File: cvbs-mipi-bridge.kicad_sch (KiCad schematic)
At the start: 114 parts, among them IC1 ADV7282-M, IC2 TLV70018, IC4 SN74AUP1G17DCKR, IC5 SN74AUP1G17DCKR, J1 WE_68715014522, J2 1053131102, J3 KLPX-0848A-2-Y, J4 KLPX-0848A-2-Y, J5 KLPX-0848A-2-Y, J6 KLPX-0848A-2-Y, J7 61300211121, Q1 BSS138PW, Q2 BSS138PW, Q3 BSS138PW, Q4 BSS138PW, Y1 ABM8G-28.63636MHZ-18-D2Y-T

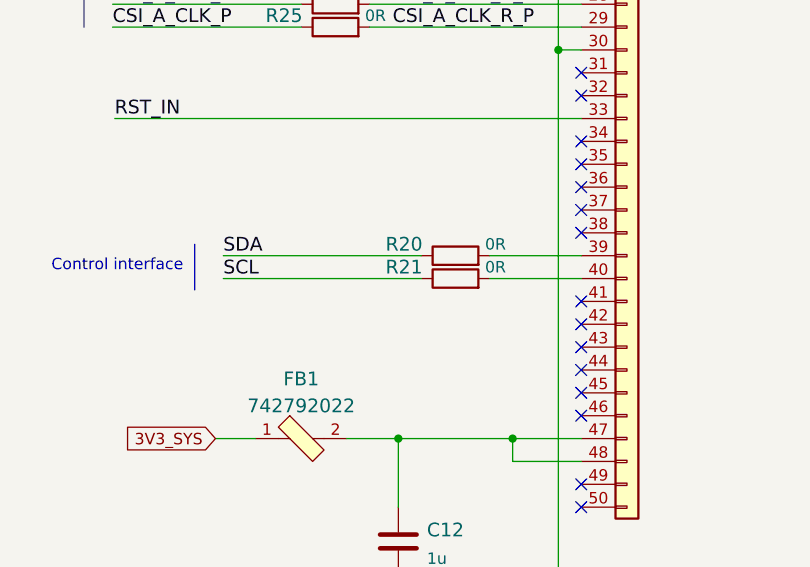
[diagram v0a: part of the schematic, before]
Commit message: Add second pair of resistors for re-connecting I2C.
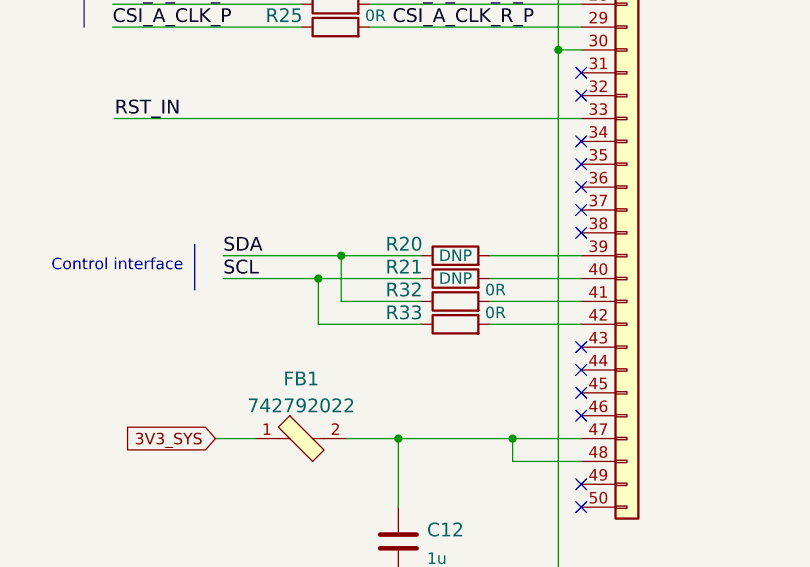
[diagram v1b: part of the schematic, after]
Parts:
- added R32, R33: R_0R_0402, cvbs-mipi-bridge-footprints:0402-res, symbol cvbs-mipi-bridge:R_0R_0402
- R20, R21: DNP (none) -> DNP
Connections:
- net SCL: now also R33.1
- net SDA: now also R32.1
- net at J1.41 (Pin_41): now also R32.2
- net at J1.42 (Pin_42): now also R33.2
- no-connect marks 35 -> 33
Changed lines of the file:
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@@
   (junction (at 363.855 155.575) (diameter 0) (color 0 0 0 0)
   )
+  (junction (at 357.505 135.255) (diameter 0) (color 0 0 0 0)
+  )
   (junction (at 193.04 50.8) (diameter 0) (color 0 0 0 0)
   )
@@
   (junction (at 381.635 74.295) (diameter 0) (color 0 0 0 0)
   )
+  (junction (at 354.965 137.795) (diameter 0) (color 0 0 0 0)
+  )
   (junction (at 113.03 36.83) (diameter 0) (color 0 0 0 0)
   )
@@
   (no_connect (at 384.175 51.435))
   (no_connect (at 384.175 56.515))
-  (no_connect (at 384.175 140.335))
-  (no_connect (at 384.175 142.875))
   (no_connect (at 384.175 86.995))
   (no_connect (at 384.175 92.075))
@@
     (stroke (width 0) (type default) (color 0 0 0 0))
   )
+  (wire (pts (xy 357.505 140.335) (xy 357.505 135.255))
+    (stroke (width 0) (type default) (color 0 0 0 0))
+  )
   (wire (pts (xy 114.935 97.79) (xy 136.525 97.79))
     (stroke (width 0) (type default) (color 0 0 0 0))
@@
     (stroke (width 0) (type default) (color 0 0 0 0))
   )
+  (wire (pts (xy 366.395 142.875) (xy 354.965 142.875))
+    (stroke (width 0) (type default) (color 0 0 0 0))
+  )
   (wire (pts (xy 275.59 86.995) (xy 276.86 86.995))
     (stroke (width 0) (type default) (color 0 0 0 0))
@@
     (stroke (width 0) (type default) (color 0 0 0 0))
   )
+  (wire (pts (xy 374.015 142.875) (xy 384.175 142.875))
+    (stroke (width 0) (type default) (color 0 0 0 0))
+  )
   (wire (pts (xy 122.555 113.03) (xy 104.775 113.03))
     (stroke (width 0) (type default) (color 0 0 0 0))
@@
     (stroke (width 0) (type default) (color 0 0 0 0))
   )
+  (wire (pts (xy 374.015 140.335) (xy 384.175 140.335))
+    (stroke (width 0) (type default) (color 0 0 0 0))
+  )
   (wire (pts (xy 200.279 140.97) (xy 200.279 146.05))
     (stroke (width 0) (type default) (color 0 0 0 0))
@@
     (stroke (width 0) (type default) (color 0 0 0 0))
   )
-  (wire (pts (xy 344.4047 135.255) (xy 366.395 135.255))
+  (wire (pts (xy 344.4047 135.255) (xy 357.505 135.255))
     (stroke (width 0) (type default) (color 0 0 0 0))
   )
@@
     (stroke (width 0) (type default) (color 0 0 0 0))
   )
+  (wire (pts (xy 354.965 137.795) (xy 366.395 137.795))
+    (stroke (width 0) (type default) (color 0 0 0 0))
+  )
   (wire (pts (xy 288.29 168.275) (xy 288.29 170.815))
     (stroke (width 0) (type default) (color 0 0 0 0))
@@
     (stroke (width 0) (type default) (color 0 0 0 0))
   )
+  (wire (pts (xy 354.965 142.875) (xy 354.965 137.795))
+    (stroke (width 0) (type default) (color 0 0 0 0))
+  )
   (wire (pts (xy 384.175 74.295) (xy 381.635 74.295))
     (stroke (width 0) (type default) (color 0 0 0 0))
@@
     (stroke (width 0) (type default) (color 0 0 0 0))
   )
+  (wire (pts (xy 357.505 135.255) (xy 366.395 135.255))
+    (stroke (width 0) (type default) (color 0 0 0 0))
+  )
   (wire (pts (xy 133.985 92.71) (xy 136.525 92.71))
     (stroke (width 0) (type default) (color 0 0 0 0))
@@
     (stroke (width 0) (type default) (color 0 0 0 0))
   )
-  (wire (pts (xy 344.4047 137.795) (xy 366.395 137.795))
+  (wire (pts (xy 344.4047 137.795) (xy 354.965 137.795))
     (stroke (width 0) (type default) (color 0 0 0 0))
   )
@@
     (stroke (width 0) (type default) (color 0 0 0 0))
   )
+  (wire (pts (xy 366.395 140.335) (xy 357.505 140.335))
+    (stroke (width 0) (type default) (color 0 0 0 0))
+  )
   (wire (pts (xy 138.43 224.155) (xy 167.64 224.155))
     (stroke (width 0) (type default) (color 0 0 0 0))
@@
       (effects (font (size 1.524 1.524)) (justify left) hide)
     )
-    (property "Val" "0R" (id 6) (at 374.65 133.985 0))
+    (property "Val" "0R" (id 6) (at 374.65 133.985 0)
+      (effects (font (size 1.27 1.27)) hide)
+    )
+    (property "DNP" "DNP" (id 7) (at 370.205 135.255 0))
     (pin "1")
     (pin "2")
@@
     (pin "1")
   )
+  (symbol (lib_id "cvbs-mipi-bridge:R_0R_0402") (at 370.205 140.335 0) (unit 1)
+    (in_bom yes) (on_board yes)
+    (property "Reference" "R32" (id 0) (at 364.49 139.065 0)
+      (effects (font (size 1.524 1.524)))
+    )
+    (property "Value" "R_0R_0402" (id 1) (at 370.205 144.145 0)
+      (effects (font (size 1.524 1.524)) hide)
+    )
+    (property "Footprint" "cvbs-mipi-bridge-footprints:0402-res" (id 2) (at 375.285 135.255 0)
+      (effects (font (size 1.524 1.524)) (justify left) hide)
+    )
+    (property "Datasheet" "" (id 3) (at 370.205 140.335 0)
+      (effects (font (size 1.27 1.27)) hide)
+    )
+    (property "Manufacturer" "PANASONIC" (id 4) (at 375.285 130.175 0)
+      (effects (font (size 1.524 1.524)) (justify left) hide)
+    )
+    (property "MPN" "ERJ2GE0R00X" (id 5) (at 375.285 132.715 0)
+      (effects (font (size 1.524 1.524)) (justify left) hide)
+    )
+    (property "Val" "0R" (id 6) (at 374.65 139.065 0))
+    (pin "1")
+    (pin "2")
+  )
   (symbol (lib_id "cvbs-mipi-bridge:GND") (at 288.29 153.67 0) (unit 1)
     (in_bom yes) (on_board yes) (fields_autoplaced)
@@
     (pin "M")
   )
+  (symbol (lib_id "cvbs-mipi-bridge:R_0R_0402") (at 370.205 142.875 0) (unit 1)
+    (in_bom yes) (on_board yes)
+    (property "Reference" "R33" (id 0) (at 364.49 141.605 0)
+      (effects (font (size 1.524 1.524)))
+    )
+    (property "Value" "R_0R_0402" (id 1) (at 370.205 146.685 0)
+      (effects (font (size 1.524 1.524)) hide)
+    )
+    (property "Footprint" "cvbs-mipi-bridge-footprints:0402-res" (id 2) (at 375.285 137.795 0)
+      (effects (font (size 1.524 1.524)) (justify left) hide)
+    )
+    (property "Datasheet" "" (id 3) (at 370.205 142.875 0)
+      (effects (font (size 1.27 1.27)) hide)
+    )
+    (property "Manufacturer" "PANASONIC" (id 4) (at 375.285 132.715 0)
+      (effects (font (size 1.524 1.524)) (justify left) hide)
+    )
+    (property "MPN" "ERJ2GE0R00X" (id 5) (at 375.285 135.255 0)
+      (effects (font (size 1.524 1.524)) (justify left) hide)
+    )
+    (property "Val" "0R" (id 6) (at 374.65 141.605 0))
+    (pin "1")
+    (pin "2")
+  )
   (symbol (lib_id "cvbs-mipi-bridge:ADV7282-M") (at 167.005 115.57 0) (unit 1)
     (in_bom yes) (on_board yes) (fields_autoplaced)
@@
       (effects (font (size 1.524 1.524)) (justify left) hide)
     )
-    (property "Val" "0R" (id 6) (at 374.65 136.525 0))
+    (property "Val" "0R" (id 6) (at 374.65 136.525 0)
+      (effects (font (size 1.27 1.27)) hide)
+    )
+    (property "DNP" "DNP" (id 7) (at 370.205 137.795 0))
     (pin "1")
     (pin "2")
@@
       (reference "R31") (unit 1) (value "R_100k_0402") (footprint "cvbs-mipi-bridge-footprints:0402-res_ThermalReliefs_ZoneSizeSettings")
     )
+    (path "/4bea3f13-01b2-4728-9623-3965c94d2e87"
+      (reference "R32") (unit 1) (value "R_0R_0402") (footprint "cvbs-mipi-bridge-footprints:0402-res")
+    )
+    (path "/5fcd8d1e-11d7-49b8-9e17-07b8242197f8"
+      (reference "R33") (unit 1) (value "R_0R_0402") (footprint "cvbs-mipi-bridge-footprints:0402-res")
+    )
     (path "/92f32a92-cb6b-49a2-8b2f-5a32a11f1e39"

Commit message: Introduce project standardization
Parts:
- removed N1: antmicro_logo, antmicro-footprints:antmicro-logo_scaled_20mm_mask, symbol cvbs-mipi-bridge:antmicro_logo
- removed N2: oshw_logo, cvbs-mipi-bridge-footprints:oshw-logo, symbol cvbs-mipi-bridge:oshw_logo
- C1, C10, C14, C16, C17, C2, C26, C29, C3, C4, C5, C6, C7: footprint cvbs-mipi-bridge-footprints:0402-cap -> cvbs-mipi-bridge-footprints:C_0402_1005Metric; Author (none) -> Antmicro; Dielectric (none) -> X5R; License (none) -> Apache-2.0; Voltage (none) -> 50V
- C11, C15, C18, C19: footprint cvbs-mipi-bridge-footprints:0402-cap -> cvbs-mipi-bridge-footprints:C_0402_1005Metric; Author (none) -> Antmicro; Dielectric (none) -> X7R; License (none) -> Apache-2.0; MPN 04025G103ZAT2A -> GRM155R71H103KA88D; Manufacturer AVX -> Murata; Voltage (none) -> 50V
- C12: footprint cvbs-mipi-bridge-footprints:0603-cap -> cvbs-mipi-bridge-footprints:C_0603_1608Metric; Author (none) -> Antmicro; License (none) -> Apache-2.0; Manufacturer WALSIN -> Walsin
- C13, C20, C21, C24: footprint cvbs-mipi-bridge-footprints:0402-cap_ThermalReliefs_ZoneSizeSettings -> cvbs-mipi-bridge-footprints:C_0402_1005Metric; Author (none) -> Antmicro; Dielectric (none) -> X5R; License (none) -> Apache-2.0; Voltage (none) -> 50V
- C22, C23: footprint cvbs-mipi-bridge-footprints:0402-cap -> cvbs-mipi-bridge-footprints:C_0402_1005Metric; Author (none) -> Antmicro; Dielectric (none) -> C0G; License (none) -> Apache-2.0; MPN MC0402N100D500CT -> GCM1555C1H100GA16D; Manufacturer MULTICOMP -> Murata; Voltage (none) -> 50V
- C25, C8, C9: footprint cvbs-mipi-bridge-footprints:0402-cap -> cvbs-mipi-bridge-footprints:C_0402_1005Metric; Author (none) -> Antmicro; License (none) -> Apache-2.0
- C27, C28: footprint cvbs-mipi-bridge-footprints:0402-cap_ThermalReliefs_ZoneSizeSettings -> cvbs-mipi-bridge-footprints:C_0402_1005Metric; Author (none) -> Antmicro; License (none) -> Apache-2.0
- C30, C31, C32: footprint cvbs-mipi-bridge-footprints:0603-cap -> cvbs-mipi-bridge-footprints:C_0603_1608Metric; Author (none) -> Antmicro; License (none) -> Apache-2.0
- D1, D2, D3, D4: Author (none) -> Antmicro; License (none) -> Apache-2.0; Manufacturer SEMTECH -> Semtech
- D5, D7, D8: value KP-1608ZGC -> LED_G_0603_KP-1608ZGC; footprint cvbs-mipi-bridge-footprints:LED_0603 -> cvbs-mipi-bridge-footprints:LED_0603_1608Metric_G; symbol cvbs-mipi-bridge:KP-1608ZGC -> cvbs-mipi-bridge:LED_G_0603_KP-1608ZGC; Author (none) -> Antmicro; License (none) -> Apache-2.0; MPN KP-1608EC -> KP-1608ZGC; Manufacturer KINGBRIGHT -> Kingbright
- D6: value KP-1608ZGC -> LED_G_0603_KP-1608ZGC; footprint cvbs-mipi-bridge-footprints:LED_0603_ThermalReliefs_ZoneSizeSettings -> cvbs-mipi-bridge-footprints:LED_0603_1608Metric_G; symbol cvbs-mipi-bridge:KP-1608ZGC -> cvbs-mipi-bridge:LED_G_0603_KP-1608ZGC; Author (none) -> Antmicro; License (none) -> Apache-2.0; MPN KP-1608EC -> KP-1608ZGC; Manufacturer KINGBRIGHT -> Kingbright
- FB1, FB3, FB4, FB5: value 742792022 -> FB_220Z_1.5A_0805; footprint cvbs-mipi-bridge-footprints:0805-res -> cvbs-mipi-bridge-footprints:FB_0805_2012Metric; symbol cvbs-mipi-bridge:742792022 -> cvbs-mipi-bridge:FB_220Z_1.5A_0805; Author (none) -> Antmicro; Current (none) -> 1.5A; License (none) -> Apache-2.0; Manufacturer Wurth Electronic -> Würth Elektronik; Val (none) -> 220Z
- IC1: Author (none) -> Antmicro; License (none) -> Apache-2.0
- IC2: value TLV70018 -> TLV70018_SC70; symbol cvbs-mipi-bridge:TLV70018 -> cvbs-mipi-bridge:TLV70018_SC70; Author (none) -> Antmicro; License (none) -> Apache-2.0
- IC4, IC5: value SN74AUP1G17DCKR -> SN74AUP1G17_SC70; footprint antmicro-footprints:SC-70-5 -> cvbs-mipi-bridge-footprints:SC-70-5; symbol cvbs-mipi-bridge:SN74AUP1G17DCKR -> cvbs-mipi-bridge:SN74AUP1G17_SC70; Author (none) -> Antmicro; License (none) -> Apache-2.0
- J1: value WE_68715014522 -> Conn_FFC_68715014522; symbol cvbs-mipi-bridge:WE_68715014522 -> cvbs-mipi-bridge:Conn_FFC_68715014522; Author (none) -> Antmicro; License (none) -> Apache-2.0; MPN 68715014522 -> 68715014522; Manufacturer Wurth Elektronik -> Würth Elektronik
- J2: value 1053131102 -> PinHeader_1x2_P2.5mm_Drill1.1mm_Shrouded_Latch; footprint cvbs-mipi-bridge-footprints:1053131102 -> cvbs-mipi-bridge-footprints:PinHeader_1x2_P2.5mm_Drill1.1mm_Shrouded_Latch; symbol cvbs-mipi-bridge:1053131102 -> cvbs-mipi-bridge:PinHeader_1x2_P2.5mm_Drill1.1mm_Shrouded_Latch; Author (none) -> Antmicro; License (none) -> Apache-2.0
- J3, J4, J5, J6: value KLPX-0848A-2-Y -> RCA_PHONO_JACK_KLPX-0848A-2-Y; footprint cvbs-mipi-bridge-footprints:KLPX-0848A-2-Y -> cvbs-mipi-bridge-footprints:RCA_PHONO_JACK_KLPX-0848A-2-Y; symbol cvbs-mipi-bridge:KLPX-0848A-2-Y -> cvbs-mipi-bridge:RCA_PHONO_JACK_KLPX-0848A-2-Y; Author (none) -> Antmicro; License (none) -> Apache-2.0; Manufacturer KYCON -> Kycon
- J7: value 61300211121 -> PinHeader_1x2_P2.54mm_Drill1.1mm; symbol cvbs-mipi-bridge:61300211121 -> cvbs-mipi-bridge:PinHeader_1x2_P2.54mm_Drill1.1mm; Author (none) -> Antmicro; License (none) -> Apache-2.0; Manufacturer Wurth Electronic -> Würth Elektronik
- MP1, MP2, MP3, MP4: value 9774030243R -> Spacer_H3mm_9774030243R; footprint cvbs-mipi-bridge-footprints:9774030243R -> cvbs-mipi-bridge-footprints:Spacer_SMD_M2_H3mm_Wurth_9774030243R; symbol cvbs-mipi-bridge:9774030243R -> cvbs-mipi-bridge:Spacer_H3mm_9774030243R; Author (none) -> Antmicro; License (none) -> Apache-2.0; Manufacturer Wurth Elektronik -> Würth Elektronik
- Q1, Q2, Q3, Q4: footprint antmicro-footprints:SC70-3 -> cvbs-mipi-bridge-footprints:SC70-3; symbol antmicroTransistorsFETsMOSFETsSingle:BSS138PW -> cvbs-mipi-bridge:BSS138PW; Author (none) -> Antmicro; License (none) -> Apache-2.0
- R1, R10, R4, R8: footprint cvbs-mipi-bridge-footprints:0402-res -> cvbs-mipi-bridge-footprints:R_0402_1005Metric; Author (none) -> Antmicro; License (none) -> Apache-2.0; MPN ERJ-2RKF24R0X -> CR0402-FX-24R0GLF; Manufacturer Panasonic -> Bourns; Tolerance (none) -> 1%
- R11, R3, R5, R9: footprint cvbs-mipi-bridge-footprints:0402-res -> cvbs-mipi-bridge-footprints:R_0402_1005Metric; Author (none) -> Antmicro; License (none) -> Apache-2.0; MPN RC0402FR-0751RL -> CR0402-FX-51R0GLF; Manufacturer YAGEO -> Bourns; Tolerance (none) -> 1%
- R12, R13, R14, R26: footprint cvbs-mipi-bridge-footprints:0402-res -> cvbs-mipi-bridge-footprints:R_0402_1005Metric; Author (none) -> Antmicro; License (none) -> Apache-2.0; MPN CRCW0402470RFKED -> CR0402-FX-4700GLF; Manufacturer VISHAY -> Bourns; Tolerance (none) -> 1%
- R15: footprint cvbs-mipi-bridge-footprints:0402-res -> cvbs-mipi-bridge-footprints:R_0402_1005Metric; Author (none) -> Antmicro; License (none) -> Apache-2.0; MPN ERJ-2RKF2202X -> CR0402-FX-2202GLF; Manufacturer Panasonic -> Bourns; Tolerance (none) -> 1%
- R16: value R_1M0_0402 -> R_1M_0402; footprint cvbs-mipi-bridge-footprints:0402-res -> cvbs-mipi-bridge-footprints:R_0402_1005Metric; symbol cvbs-mipi-bridge:R_1M0_0402 -> cvbs-mipi-bridge:R_1M_0402; Author (none) -> Antmicro; License (none) -> Apache-2.0; MPN CRG0402F1M0 -> CR0402-FX-1004GLF; Manufacturer TE CONNECTIVITY -> Bourns; Tolerance (none) -> 1%; Val 1M0 -> 1M
- R17, R18, R19: footprint cvbs-mipi-bridge-footprints:0402-res -> cvbs-mipi-bridge-footprints:R_0402_1005Metric; Author (none) -> Antmicro; License (none) -> Apache-2.0; MPN CRCW0402100KFKEDHP -> CR0402-FX-1003GLF; Manufacturer VISHAY -> Bourns; Tolerance (none) -> 1%
- R2: footprint cvbs-mipi-bridge-footprints:0402-res -> cvbs-mipi-bridge-footprints:R_0402_1005Metric; Author (none) -> Antmicro; License (none) -> Apache-2.0; Manufacturer BOURNS -> Bourns; Tolerance (none) -> 1%
- R20, R21, R22, R23, R24, R25, R32, R33: footprint cvbs-mipi-bridge-footprints:0402-res -> cvbs-mipi-bridge-footprints:R_0402_1005Metric; Author (none) -> Antmicro; Current (none) -> 1A; License (none) -> Apache-2.0; Manufacturer PANASONIC -> Panasonic
- R27, R28, R29, R31: footprint cvbs-mipi-bridge-footprints:0402-res_ThermalReliefs_ZoneSizeSettings -> cvbs-mipi-bridge-footprints:R_0402_1005Metric; Author (none) -> Antmicro; License (none) -> Apache-2.0; MPN CRCW0402100KFKEDHP -> CR0402-FX-1003GLF; Manufacturer VISHAY -> Bourns; Tolerance (none) -> 1%
- R30: footprint cvbs-mipi-bridge-footprints:0805-res -> cvbs-mipi-bridge-footprints:R_0805_2012Metric; Author (none) -> Antmicro; Current (none) -> 2.5A; License (none) -> Apache-2.0; Manufacturer VISHAY -> Vishay
- R6, R7: footprint cvbs-mipi-bridge-footprints:0402-res -> cvbs-mipi-bridge-footprints:R_0402_1005Metric; Author (none) -> Antmicro; License (none) -> Apache-2.0; MPN MCS04020C4701FE000 -> CR0402-FX-4701GLF; Manufacturer VISHAY -> Bourns; Tolerance (none) -> 1%; now in the parts list
- S1: value KMR2 -> SW_SPST_KMR211NGLFS; footprint cvbs-mipi-bridge-footprints:SW_SPST_4.2x2.8_ThermalReliefs_ZoneSizeSettings -> cvbs-mipi-bridge-footprints:SW_SPST_4.2x2.8; symbol cvbs-mipi-bridge:KMR2 -> cvbs-mipi-bridge:SW_SPST_KMR211NGLFS; Author (none) -> Antmicro; License (none) -> Apache-2.0; Manufacturer C&K Components -> C&K
- TP1, TP10, TP11, TP12, TP13, TP14, TP15, TP16, TP2, TP3, TP4, TP5, TP6, TP7, TP8, TP9: value TP -> TP_1.5mm_SMD; footprint cvbs-mipi-bridge-footprints:TP-R-1.5 -> cvbs-mipi-bridge-footprints:TP_SMD_1.5mm; symbol cvbs-mipi-bridge:TP -> cvbs-mipi-bridge:TP_1.5mm_SMD; Author (none) -> Antmicro; License (none) -> Apache-2.0
- Y1: value ABM8G-28.63636MHZ-18-D2Y-T -> Oscillator_SMD_28.63636MHz_KX-7; footprint cvbs-mipi-bridge-footprints:KX-7 -> cvbs-mipi-bridge-footprints:Oscillator_SMD_Geyer_KX-7-4Pin_3.2x2.5mm; symbol cvbs-mipi-bridge:ABM8G-28.63636MHZ-18-D2Y-T -> cvbs-mipi-bridge:Oscillator_SMD_28.63636MHz_KX-7; Author (none) -> Antmicro; License (none) -> Apache-2.0; MPN ABM8G-25.000MHZ-18-D2Y-T -> ABM8G-28.63636MHZ-18-D2Y-T
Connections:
- net 1V8_SYS: now also C26.1; no longer C26.2
- net 3V3_SYS: now also C24.2, C27.2, C29.1, C5.1, C7.1; no longer C24.1, C27.1, C29.2, C5.2, C7.2
- net AIN1_ESD: now also D1.2 (A); no longer D1.K
- net AIN2_ESD: now also D2.2 (A); no longer D2.K
- net AIN3_ESD: now also D3.2 (A); no longer D3.K
- net AIN4_ESD: now also D4.2 (A); no longer D4.K
- net AVDD_1V8: now also C14.1, C15.2; no longer C14.2, C15.1
- net DVDD_1V8: now also C16.1, C17.1, C18.2; no longer C16.2, C17.2, C18.1
- net PVDD_1V8: now also C11.2, C3.1; no longer C11.1, C3.2
- net VREFN: now also C6.2; no longer C6.1
- net VREFP: now also C6.1; no longer C6.2
- net at IC4.2 (A), R15.1: now also C13.2; no longer C13.1
- net GND renamed DGND
- net DGND: now also C11.1, C13.1, C14.2, C15.1, C16.2, C17.2, C18.1, C24.1, C26.2, C27.1, C29.2, C3.2, C5.2, C7.2, D1.1 (K), D2.1 (K), D3.1 (K), D4.1 (K); no longer C11.2, C13.2, C14.1, C15.2, C16.1, C17.1, C18.2, C24.2, C26.1, C27.2, C29.1, C3.1, C5.1, C7.1, D1.A, D2.A, D3.A, D4.A
- no-connect marks 33 -> 37
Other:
- moved on the sheet: C1, C10, C11, C12, C13, C14, C15, C16, C17, C18, C19, C2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

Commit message: [#56797] Fix lib references
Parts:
- C1, C10, C13, C14, C16, C17, C2, C20, C21, C24, C26, C29, C3, C4, C5, C6, C7: footprint cvbs-mipi-bridge-footprints:C_0402_1005Metric -> antmicro-footprints:C_0402_1005Metric; symbol cvbs-mipi-bridge:C_100n_0402 -> antmicroCapacitors0402:C_100n_0402
- C11, C15, C18, C19: footprint cvbs-mipi-bridge-footprints:C_0402_1005Metric -> antmicro-footprints:C_0402_1005Metric; symbol cvbs-mipi-bridge:C_10n_0402 -> antmicroCapacitors0402:C_10n_0402
- C12: footprint cvbs-mipi-bridge-footprints:C_0603_1608Metric -> antmicro-footprints:C_0603_1608Metric; symbol cvbs-mipi-bridge:C_1u_0603 -> antmicroCapacitors0603:C_1u_0603
- C22, C23: footprint cvbs-mipi-bridge-footprints:C_0402_1005Metric -> antmicro-footprints:C_0402_1005Metric; symbol cvbs-mipi-bridge:C_10p_0402 -> antmicroCapacitors0402:C_10p_0402
- C25, C27, C28, C8, C9: footprint cvbs-mipi-bridge-footprints:C_0402_1005Metric -> antmicro-footprints:C_0402_1005Metric; symbol cvbs-mipi-bridge:C_1u_0402 -> antmicroCapacitors0402:C_1u_0402
- C30, C31, C32: footprint cvbs-mipi-bridge-footprints:C_0603_1608Metric -> antmicro-footprints:C_0603_1608Metric; symbol cvbs-mipi-bridge:C_10u_0603 -> antmicroCapacitors0603:C_10u_0603
- D1, D2, D3, D4: footprint cvbs-mipi-bridge-footprints:SLP1006P2T -> antmicro-footprints:SLP1006P2T; symbol cvbs-mipi-bridge:UCLAMP2501T.TCT -> antmicroTVSDiodes:UCLAMP2501T.TCT
- D5, D6, D7, D8: footprint cvbs-mipi-bridge-footprints:LED_0603_1608Metric_G -> antmicro-footprints:LED_0603_1608Metric_G; symbol cvbs-mipi-bridge:LED_G_0603_KP-1608ZGC -> antmicroLEDIndicationDiscrete:LED_G_0603_KP-1608ZGC
- FB1, FB3, FB4, FB5: value FB_220Z_1.5A_0805 -> FB_220Z_1.5A_WE-CBF_0805; footprint cvbs-mipi-bridge-footprints:FB_0805_2012Metric -> antmicro-footprints:FB_0805_2012Metric; symbol cvbs-mipi-bridge:FB_220Z_1.5A_0805 -> antmicroFerriteBeadsandChips:FB_220Z_1.5A_WE-CBF_0805; Current 1.5A -> (none); Val 220Z -> 220Z/1.5A
- IC1: footprint cvbs-mipi-bridge-footprints:LFCSP-32-1EP-5x5mm -> antmicro-footprints:LFCSP-32-1EP-5x5mm; symbol cvbs-mipi-bridge:ADV7282-M -> antmicroDataAcquisitionAnalogtoDigitalConvertersADC:ADV7282-M
- IC2: footprint cvbs-mipi-bridge-footprints:SC-70-5 -> antmicro-footprints:SC-70-5; symbol cvbs-mipi-bridge:TLV70018_SC70 -> antmicroPMICVoltageRegulatorsLinear:TLV70018_SC70
- IC4, IC5: footprint cvbs-mipi-bridge-footprints:SC-70-5 -> antmicro-footprints:SC-70-5; symbol cvbs-mipi-bridge:SN74AUP1G17_SC70 -> antmicroLogicBuffersDriversReceiversTransceivers:SN74AUP1G17_SC70
- J1: value Conn_FFC_68715014522 -> Conn_FFC_WE_68715014522; footprint cvbs-mipi-bridge-footprints:WE_68715014522 -> antmicro-footprints:Conn_FFC_WE_68715014x22; symbol cvbs-mipi-bridge:Conn_FFC_68715014522 -> antmicroFCCConnectors:Conn_FFC_WE_68715014522; VSD_Class (none) -> Antmicro Dual Camera interface
- J2: value PinHeader_1x2_P2.5mm_Drill1.1mm_Shrouded_Latch -> Molex_Nano-Fit_1x2_1053131102; footprint cvbs-mipi-bridge-footprints:PinHeader_1x2_P2.5mm_Drill1.1mm_Shrouded_Latch -> antmicro-footprints:Conn_Molex_Nano-Fit_1x2_1053131102; symbol cvbs-mipi-bridge:PinHeader_1x2_P2.5mm_Drill1.1mm_Shrouded_Latch -> antmicroWire2BoardConnectors:Molex_Nano-Fit_1x2_1053131102
- J3, J4, J5, J6: value RCA_PHONO_JACK_KLPX-0848A-2-Y -> RCA_Jack_KLPX-0848A-2-Y; footprint cvbs-mipi-bridge-footprints:RCA_PHONO_JACK_KLPX-0848A-2-Y -> antmicro-footprints:RCA_Jack_KLPX-0848A-2-Y; symbol cvbs-mipi-bridge:RCA_PHONO_JACK_KLPX-0848A-2-Y -> antmicroBarrelAudioConnectors:RCA_Jack_KLPX-0848A-2-Y
- J7: footprint cvbs-mipi-bridge-footprints:PinHeader_1x2_P2.54_Drill0.9mm -> antmicro-footprints:PinHeader_1x2_P2.54_Drill0.9mm; symbol cvbs-mipi-bridge:PinHeader_1x2_P2.54mm_Drill1.1mm -> antmicroGenericPinHeaders:PinHeader_1x2_P2.54mm_Drill1.1mm
- MP1, MP2, MP3, MP4: value Spacer_H3mm_9774030243R -> Spacer_Drill3mm_H3mm_9774030243R; footprint cvbs-mipi-bridge-footprints:Spacer_SMD_M2_H3mm_Wurth_9774030243R -> antmicro-footprints:Spacer_Drill3mm_H3mm_9774030243R; symbol cvbs-mipi-bridge:Spacer_H3mm_9774030243R -> antmicroMechanicalParts:Spacer_Drill3mm_H3mm_9774030243R
- Q1, Q2, Q3, Q4: footprint cvbs-mipi-bridge-footprints:SC70-3 -> antmicro-footprints:SC70-3; symbol cvbs-mipi-bridge:BSS138PW -> antmicroTransistorsFETsMOSFETsSingle:BSS138PW
- R1, R10, R4, R8: footprint cvbs-mipi-bridge-footprints:R_0402_1005Metric -> antmicro-footprints:R_0402_1005Metric; symbol cvbs-mipi-bridge:R_24R_0402 -> antmicroResistors0402:R_24R_0402
- R11, R3, R5, R9: footprint cvbs-mipi-bridge-footprints:R_0402_1005Metric -> antmicro-footprints:R_0402_1005Metric; symbol cvbs-mipi-bridge:R_51R_0402 -> antmicroResistors0402:R_51R_0402
- R12, R13, R14, R26: footprint cvbs-mipi-bridge-footprints:R_0402_1005Metric -> antmicro-footprints:R_0402_1005Metric; symbol cvbs-mipi-bridge:R_470R_0402 -> antmicroResistors0402:R_470R_0402
- R15: footprint cvbs-mipi-bridge-footprints:R_0402_1005Metric -> antmicro-footprints:R_0402_1005Metric; symbol cvbs-mipi-bridge:R_22k_0402 -> antmicroResistors0402:R_22k_0402
- R16: footprint cvbs-mipi-bridge-footprints:R_0402_1005Metric -> antmicro-footprints:R_0402_1005Metric; symbol cvbs-mipi-bridge:R_1M_0402 -> antmicroResistors0402:R_1M_0402
- R17, R18, R19, R27, R28, R29, R31: footprint cvbs-mipi-bridge-footprints:R_0402_1005Metric -> antmicro-footprints:R_0402_1005Metric; symbol cvbs-mipi-bridge:R_100k_0402 -> antmicroResistors0402:R_100k_0402
- R2: footprint cvbs-mipi-bridge-footprints:R_0402_1005Metric -> antmicro-footprints:R_0402_1005Metric; symbol cvbs-mipi-bridge:R_1k_0402 -> antmicroResistors0402:R_1k_0402
- R20, R21, R22, R23, R24, R25, R32, R33: footprint cvbs-mipi-bridge-footprints:R_0402_1005Metric -> antmicro-footprints:R_0402_1005Metric; symbol cvbs-mipi-bridge:R_0R_0402 -> antmicroResistors0402:R_0R_0402
- R30: footprint cvbs-mipi-bridge-footprints:R_0805_2012Metric -> antmicro-footprints:R_0805_2012Metric; symbol cvbs-mipi-bridge:R_0R_0805 -> antmicroResistorsmisc:R_0R_0805
- R6, R7: footprint cvbs-mipi-bridge-footprints:R_0402_1005Metric -> antmicro-footprints:R_0402_1005Metric; symbol cvbs-mipi-bridge:R_4k7_0402 -> antmicroResistors0402:R_4k7_0402
- S1: value SW_SPST_KMR211NGLFS -> SW_KMR211NGLFS_SMD; footprint cvbs-mipi-bridge-footprints:SW_SPST_4.2x2.8 -> antmicro-footprints:SW_KMR211NGLFS_SMD; symbol cvbs-mipi-bridge:SW_SPST_KMR211NGLFS -> antmicroPushbuttonSwitches:SW_KMR211NGLFS_SMD
- TP1, TP10, TP11, TP12, TP13, TP14, TP15, TP16, TP2, TP3, TP4, TP5, TP6, TP7, TP8, TP9: footprint cvbs-mipi-bridge-footprints:TP_SMD_1.5mm -> antmicro-footprints:TP_SMD_1.5mm; symbol cvbs-mipi-bridge:TP_1.5mm_SMD -> antmicroTestPoints:TP_1.5mm_SMD
- Y1: value Oscillator_SMD_28.63636MHz_KX-7 -> Resonator_28.63636MHz_ABM8G; footprint cvbs-mipi-bridge-footprints:Oscillator_SMD_Geyer_KX-7-4Pin_3.2x2.5mm -> antmicro-footprints:Oscillator_SMD_Geyer_KX-7-4Pin_3.2x2.5mm; symbol cvbs-mipi-bridge:Oscillator_SMD_28.63636MHz_KX-7 -> antmicroResonators:Resonator_28.63636MHz_ABM8G; Val (none) -> 28.63636 MHz
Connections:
- net AIN1_ESD: now also J3.1; no longer J3.2
- net AIN2_ESD: now also J4.1; no longer J4.2
- net AIN3_ESD: now also J5.1; no longer J5.2
- net AIN4_ESD: now also J6.1; no longer J6.2
- net DGND: now also J1.MP1 (MP), J1.MP2 (MP), J3.2, J4.2, J5.2, J6.2, S1.2; no longer J3.1, J4.1, J5.1, J6.1, S1.3
- net at C21.1, IC5.2 (A), Q1.3 (D)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: now also S1.3; no longer S1.2
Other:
- moved on the sheet: C12, C13, C14, C15, C17, C18, C19, C20, C21, C22, C24, C25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
